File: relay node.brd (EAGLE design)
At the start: 67.8 x 40.6 mm, 25 parts, among them J1 Channels, J2 LED, J3 PROG, J4 AUX, U1 ESP-WROOM-02U, U2 MCP23018-E/SO, U3 TLV75533

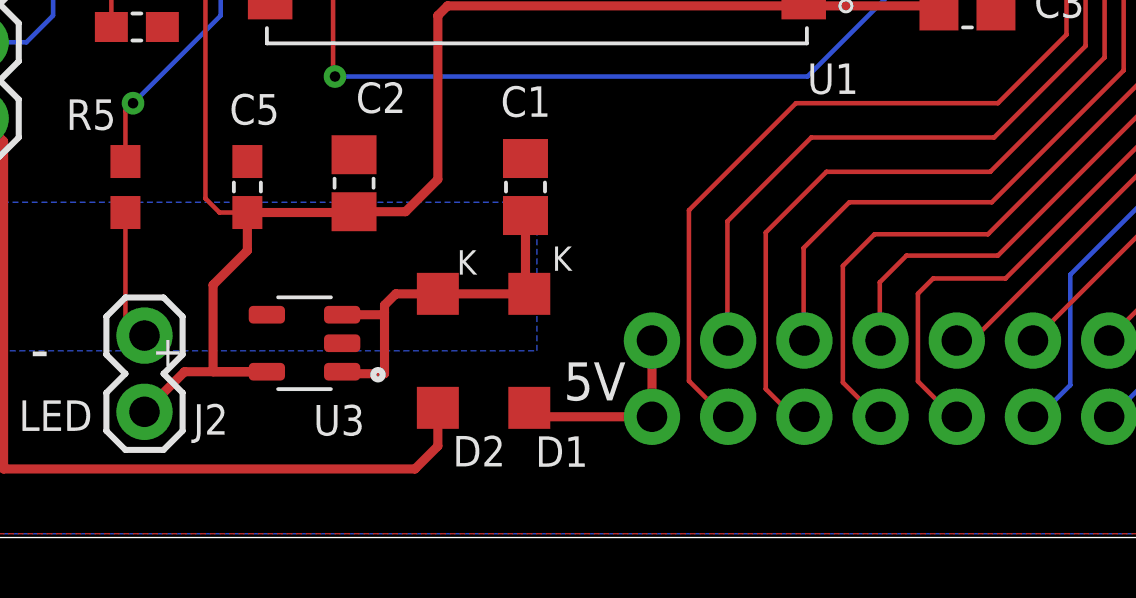
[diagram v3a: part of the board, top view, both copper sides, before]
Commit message: Replace volt regulator
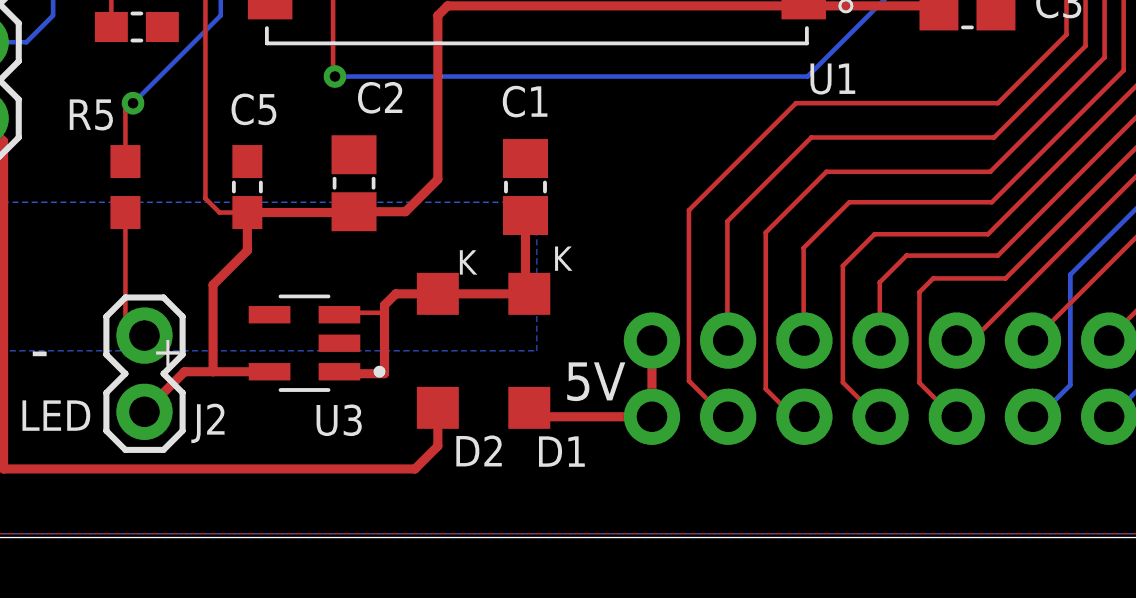
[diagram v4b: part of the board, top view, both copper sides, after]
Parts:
- U3: value TLV75533 -> MIC5504-3.3
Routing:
- net 3.3V: track 123.1 -> 121.4 mm
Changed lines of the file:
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@@
 </autorouter>
 <elements>
-<element name="U3" library="SFM-Project" package="SOT95P280X145-5N" value="TLV75533" x="16.891" y="6.477" smashed="yes" rot="R180">
-<attribute name="DESCRIPTION" value=" Linear Voltage Regulator IC 1 Output 500mA SOT-23-5 " x="16.891" y="6.477" size="1.778" layer="27" rot="R180" display="off"/>
-<attribute name="DIGI-KEY_PART_NUMBER" value="296-50411-1-ND" x="16.891" y="6.477" size="1.778" layer="27" rot="R180" display="off"/>
-<attribute name="DIGI-KEY_PURCHASE_URL" value="https://www.digikey.com/product-detail/en/texas-instruments/TLV75533PDBVR/296-50411-1-ND/9685550?utm_source=snapeda&amp;utm_medium=aggregator&amp;utm_campaign=symbol" x="16.891" y="6.477" size="1.778" layer="27" rot="R180" display="off"/>
-<attribute name="MF" value="Texas Instruments" x="16.891" y="6.477" size="1.778" layer="27" rot="R180" display="off"/>
-<attribute name="MP" value="TLV75533PDBVR" x="16.891" y="6.477" size="1.778" layer="27" rot="R180" display="off"/>
-<attribute name="NAME" x="18.8997" y="4.41808125" size="1.016" layer="25" rot="R180"/>
-<attribute name="PACKAGE" value="SOT-23 Texas Instruments" x="16.891" y="6.477" size="1.778" layer="27" rot="R180" display="off"/>
-<attribute name="VALUE" x="18.94726875" y="9.385859375" size="1.019109375" layer="27" rot="R180"/>
+<element name="U3" library="SFM-Project" package="SOT95P280X145-5N" value="MIC5504-3.3" x="16.891" y="6.477" locked="yes" smashed="yes" rot="R180">
+<attribute name="DESCRIPTION" value=" Linear Voltage Regulator IC 1 Output 300mA SOT-23-5 " x="16.891" y="6.477" locked="yes" size="1.778" layer="27" rot="R180" display="off"/>
+<attribute name="DIGI-KEY_PART_NUMBER" value="MIC5504-3.3YM5-T5CT-ND" x="16.891" y="6.477" locked="yes" size="1.778" layer="27" rot="R180" display="off"/>
+<attribute name="DIGIKEY-PURCHASE-URL" value="https://snapeda.com/shop?store=DigiKey&amp;id=1219468" x="16.891" y="6.477" locked="yes" size="1.778" layer="27" rot="R180" display="off"/>
+<attribute name="MF" value="Microchip" x="16.891" y="6.477" locked="yes" size="1.778" layer="27" rot="R180" display="off"/>
+<attribute name="MP" value="MIC5504-3.3YM5-T5" x="16.891" y="6.477" locked="yes" size="1.778" layer="27" rot="R180" display="off"/>
+<attribute name="NAME" x="18.8997" y="4.41808125" locked="yes" size="1.016" layer="25" rot="R180"/>
+<attribute name="PACKAGE" value="SOT-23-5 Microchip" x="16.891" y="6.477" locked="yes" size="1.778" layer="27" rot="R180" display="off"/>
+<attribute name="VALUE" x="18.94726875" y="9.385859375" locked="yes" size="1.019109375" layer="27" rot="R180"/>
 </element>
 <element name="J2" library="SFM-Project" package="1X02" value="LED" x="11.557" y="4.191" locked="yes" smashed="yes" rot="R90">
@@
 <contactref element="C1" pad="2"/>
 <contactref element="C2" pad="2"/>
-<contactref element="C3" pad="2"/>
-<contactref element="C4" pad="2"/>
 <contactref element="C5" pad="2"/>
 <contactref element="C8" pad="2"/>
 <contactref element="C9" pad="2"/>
-<contactref element="C6" pad="2"/>
-<contactref element="C7" pad="2"/>
 <contactref element="J4" pad="4"/>
 <via x="41.275" y="29.337" extent="1-16" drill="0.35"/>
@@
 <vertex x="24.638" y="11.176"/>
 </polygon>
+<contactref element="C3" pad="2"/>
+<contactref element="C6" pad="2"/>
+<contactref element="C4" pad="2"/>
+<contactref element="C7" pad="2"/>
 </signal>
 <signal name="3.3V">
-<contactref element="U3" pad="5"/>
 <contactref element="R1" pad="2"/>
 <contactref element="R4" pad="2"/>
@@
 <contactref element="C7" pad="1"/>
 <wire x1="12.893" y1="5.527" x2="11.557" y2="4.191" width="0.3048" layer="1"/>
-<wire x1="15.636" y1="5.527" x2="12.893" y2="5.527" width="0.3048" layer="1"/>
-<wire x1="15.636" y1="5.527" x2="13.843" y2="5.527" width="0.3048" layer="1"/>
 <wire x1="14.986" y1="9.564" x2="13.843" y2="8.421" width="0.3048" layer="1"/>
 <wire x1="14.986" y1="9.564" x2="14.986" y2="10.834" width="0.3048" layer="1"/>
@@
 <wire x1="62.318" y1="31.203" x2="62.318" y2="31.877" width="0.1524" layer="1"/>
 <wire x1="60.745" y1="30.773" x2="60.96" y2="30.988" width="0.1524" layer="1"/>
+<contactref element="U3" pad="5"/>
+<wire x1="15.726" y1="5.527" x2="13.843" y2="5.527" width="0.3048" layer="1"/>
+<wire x1="13.843" y1="5.527" x2="12.893" y2="5.527" width="0.3048" layer="1"/>
 </signal>
 <signal name="+5V">
@@
 <signal name="CH7">
 <contactref element="U2" pad="26"/>
-<wire x1="37.846" y1="8.636" x2="37.338" y2="8.128" width="0.1524" layer="1"/>
-<wire x1="37.338" y1="8.128" x2="37.338" y2="5.207" width="0.1524" layer="1"/>
+<wire x1="37.846" y1="8.636" x2="37.3888" y2="8.1788" width="0.1524" layer="1"/>
+<wire x1="37.3888" y1="8.1788" x2="37.3888" y2="5.1562" width="0.1524" layer="1"/>
 <wire x1="37.846" y1="8.636" x2="40.259" y2="8.636" width="0.1524" layer="1"/>
 <contactref element="J1" pad="10"/>
-<wire x1="37.338" y1="5.207" x2="38.5191" y2="4.0259" width="0.1524" layer="1"/>
+<wire x1="37.3888" y1="5.1562" x2="38.5191" y2="4.0259" width="0.1524" layer="1"/>
 <wire x1="38.5191" y1="4.0259" x2="38.6334" y2="4.0259" width="0.1524" layer="1"/>
 <wire x1="40.259" y1="8.636" x2="46.101" y2="14.478" width="0.1524" layer="1"/>
@@
 </signal>
 <signal name="N$1">
-<contactref element="U3" pad="1"/>
-<contactref element="D1" pad="C"/>
-<contactref element="U3" pad="3"/>
 <contactref element="D2" pad="C"/>
 <contactref element="C1" pad="1"/>
-<wire x1="24.384" y1="8.123" x2="24.257" y2="8.123" width="0.3048" layer="1"/>
-<wire x1="24.257" y1="8.123" x2="21.336" y2="8.123" width="0.3048" layer="1"/>
 <wire x1="21.331" y1="8.128" x2="21.336" y2="8.123" width="0.3048" layer="1"/>
 <wire x1="21.336" y1="8.123" x2="19.934" y2="8.123" width="0.3048" layer="1"/>
@@
 <wire x1="19.558" y1="7.747" x2="19.558" y2="7.493" width="0.3048" layer="1"/>
 <wire x1="19.558" y1="7.493" x2="19.558" y2="5.461" width="0.3048" layer="1"/>
-<wire x1="19.558" y1="5.461" x2="18.212" y2="5.461" width="0.3048" layer="1"/>
-<wire x1="18.212" y1="5.461" x2="18.146" y2="5.527" width="0.3048" layer="1"/>
-<wire x1="18.146" y1="7.427" x2="19.492" y2="7.427" width="0.3048" layer="1"/>
-<wire x1="19.492" y1="7.427" x2="19.558" y2="7.493" width="0.3048" layer="1"/>
-<wire x1="24.257" y1="10.734" x2="24.257" y2="8.123" width="0.3048" layer="1"/>
+<contactref element="D1" pad="C"/>
+<contactref element="U3" pad="1"/>
+<contactref element="U3" pad="3"/>
+<wire x1="19.558" y1="5.461" x2="18.122" y2="5.461" width="0.3048" layer="1"/>
+<wire x1="18.122" y1="5.461" x2="18.056" y2="5.527" width="0.3048" layer="1"/>
+<wire x1="18.056" y1="7.427" x2="18.122" y2="7.493" width="0.1524" layer="1"/>
+<wire x1="18.122" y1="7.493" x2="19.558" y2="7.493" width="0.1524" layer="1"/>
+<wire x1="21.336" y1="8.123" x2="24.384" y2="8.123" width="0.3048" layer="1"/>
+<wire x1="24.384" y1="8.123" x2="24.257" y2="8.25" width="0.3048" layer="1"/>
+<wire x1="24.257" y1="8.25" x2="24.257" y2="10.734" width="0.3048" layer="1"/>
 </signal>
 <signal name="+5V_PROG">
@@
 <wire x1="35.478" y1="19.222" x2="36.449" y2="20.193" width="0.1524" layer="1"/>
 </signal>
+<signal name="OUT">
+</signal>
 </signals>

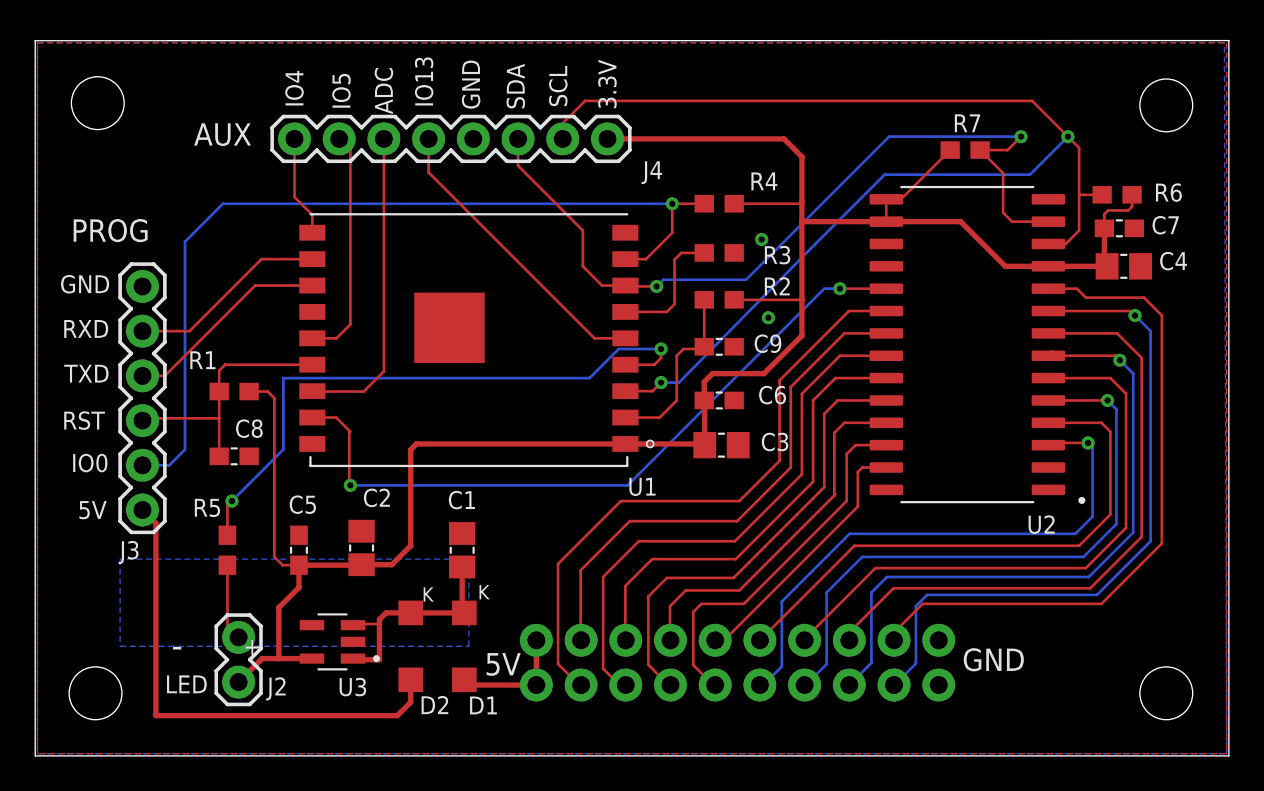
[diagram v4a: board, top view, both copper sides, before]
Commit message: Minor changes for production PCB ordered -  v1.0.0
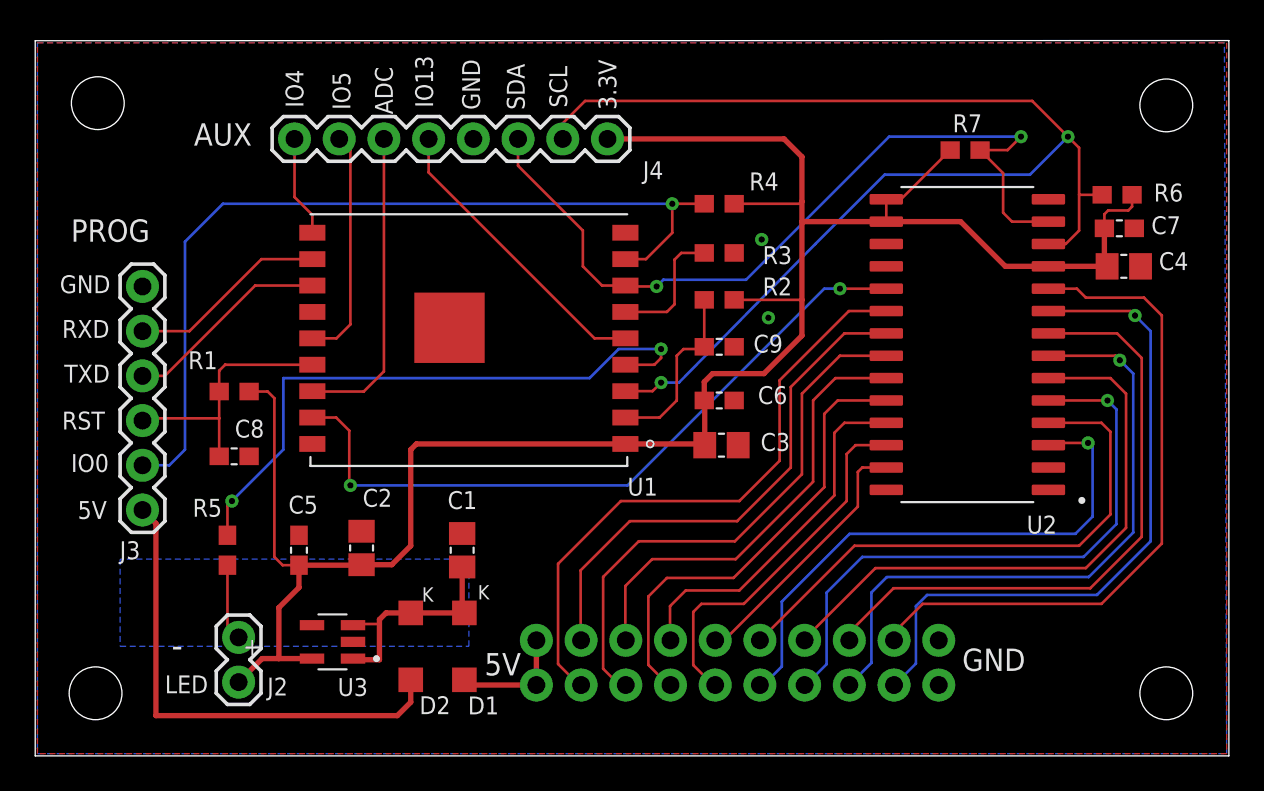
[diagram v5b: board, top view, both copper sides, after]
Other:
- board text added: "RELAY NODE v1.0.0"
- board text removed: "RELAY NODE v2.1.0"
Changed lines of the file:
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@@
 <text x="25.527" y="4.572" size="1.27" layer="25">5V</text>
 <text x="24.003" y="6.477" size="1.6764" layer="42" font="vector" rot="MR0">RELAY NODE
-v2.1.0</text>
+v1.0.0</text>
 <text x="21.971" y="8.763" size="0.8128" layer="25">K</text>
 <text x="25.146" y="8.89" size="0.8128" layer="25">K</text>
@@
 <contactref element="J1" pad="1"/>
 <contactref element="J1" pad="2"/>
-<wire x1="24.7319" y1="3.9751" x2="24.384" y2="4.323" width="0.3048" layer="1"/>
 <wire x1="28.4734" y1="6.5659" x2="28.4734" y2="4.0259" width="0.3048" layer="1"/>
 <wire x1="28.4734" y1="4.0259" x2="24.6811" y2="4.0259" width="0.3048" layer="1"/>
@@
 <wire x1="36.066840625" y1="6.592459375" x2="36.0934" y2="6.5659" width="0.1524" layer="1"/>
 <wire x1="40.005" y1="9.398" x2="45.4025" y2="14.7955" width="0.1524" layer="1"/>
-<wire x1="45.4025" y1="14.7955" x2="45.466" y2="14.859" width="0.1524" layer="1"/>
 <wire x1="45.4025" y1="14.7955" x2="45.4025" y2="18.3515" width="0.1524" layer="1"/>
 <wire x1="45.4025" y1="18.3515" x2="45.974" y2="18.923" width="0.1524" layer="1"/>
@@
 <contactref element="U2" pad="27"/>
 <contactref element="J1" pad="9"/>
-<wire x1="38.6334" y1="6.5659" x2="38.6334" y2="6.6104" width="0.1524" layer="1"/>
-<wire x1="38.6334" y1="6.5659" x2="39.1414" y2="6.5659" width="0.1524" layer="1"/>
-<wire x1="46.736" y1="14.1605" x2="39.1414" y2="6.5659" width="0.1524" layer="1"/>
+<wire x1="39.1414" y1="6.5659" x2="46.736" y2="14.1605" width="0.1524" layer="1"/>
 <wire x1="46.736" y1="14.1605" x2="46.736" y2="16.129" width="0.1524" layer="1"/>
 <wire x1="46.736" y1="16.129" x2="46.99" y2="16.383" width="0.1524" layer="1"/>
 <wire x1="46.99" y1="16.383" x2="48.354" y2="16.383" width="0.1524" layer="1"/>
+<wire x1="38.6334" y1="6.5659" x2="39.1414" y2="6.5659" width="0.1524" layer="1"/>
 </signal>
 <signal name="CH9">
@@
 <contactref element="J1" pad="16"/>
 <wire x1="57.564" y1="22.733" x2="57.611" y2="22.78" width="0.1524" layer="1"/>
-<wire x1="57.611" y1="22.78" x2="57.818" y2="22.987" width="0.1524" layer="1"/>
 <wire x1="61.6232" y1="22.479" x2="61.3692" y2="22.733" width="0.1524" layer="1"/>
 <wire x1="61.3692" y1="22.733" x2="57.658" y2="22.733" width="0.1524" layer="1"/>
@@
 <wire x1="50.419" y1="8.636" x2="48.7934" y2="7.0104" width="0.1524" layer="1"/>
 <wire x1="48.7934" y1="7.0104" x2="48.7934" y2="6.5659" width="0.1524" layer="1"/>
-<wire x1="57.691" y1="26.67" x2="57.564" y2="26.543" width="0.1524" layer="1"/>
 <wire x1="57.564" y1="26.543" x2="59.182" y2="26.543" width="0.1524" layer="1"/>
 <wire x1="59.182" y1="26.543" x2="59.69" y2="26.035" width="0.1524" layer="1"/>
@@
 <wire x1="15.7455" y1="19.222" x2="17.1" y2="19.222" width="0.1524" layer="1"/>
 <wire x1="17.1" y1="19.222" x2="17.8435" y2="18.4785" width="0.1524" layer="1"/>
-<wire x1="17.8435" y1="18.4785" x2="17.907" y2="18.415" width="0.1524" layer="1"/>
 <wire x1="17.8435" y1="18.4785" x2="17.8435" y2="15.4305" width="0.1524" layer="1"/>
 <wire x1="17.8435" y1="15.4305" x2="17.907" y2="15.367" width="0.1524" layer="1"/>
